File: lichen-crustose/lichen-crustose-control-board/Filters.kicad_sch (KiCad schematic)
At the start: 11 parts, among them J5 Thonkiconn_Mono_Audio_Jack, J6 Thonkiconn_Mono_Audio_Jack, U1 NSL-32SR3, U2 NS-32SR2

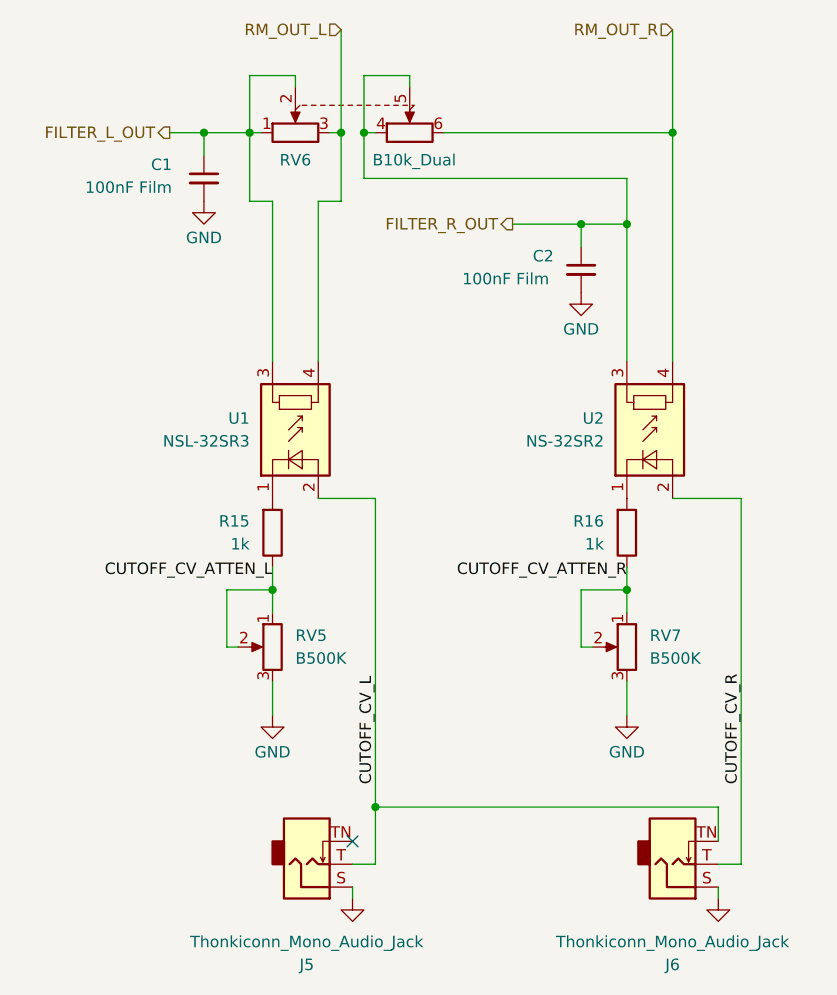
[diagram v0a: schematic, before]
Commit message: Updates Lichen symbols and footprints. Fixes to Crustose and Vactrol VCA. Adds 3D model of the RP2350 dual USB board.
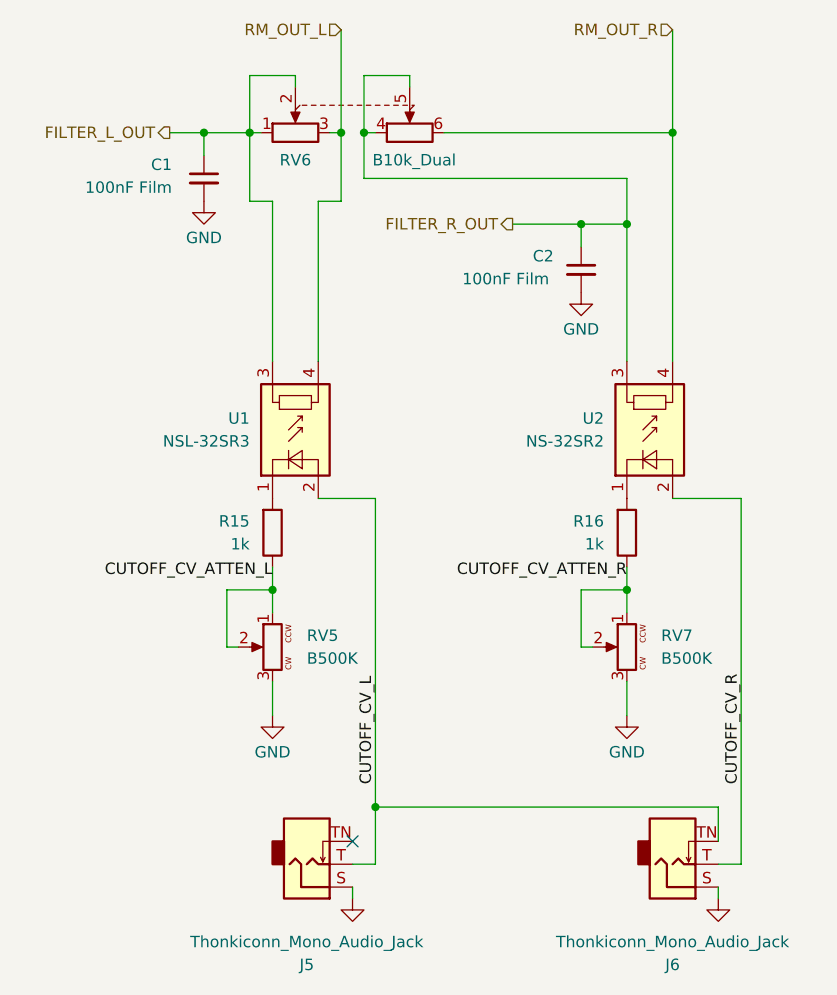
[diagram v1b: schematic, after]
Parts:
- J5, J6, RV6, U1, U2: now left out of the parts list
- R15, R16: value 10k_0603 -> 1k_0603; JLCPCB ID C25804 -> (none)
- RV5, RV7: symbol Lichen:Potentiometer -> Lichen:R_Potentiometer; now left out of the parts list
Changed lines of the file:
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@@
 		(unit 1)
 		(exclude_from_sim no)
-		(in_bom yes)
+		(in_bom no)
 		(on_board yes)
 		(dnp no)
@@
 		(unit 1)
 		(exclude_from_sim no)
-		(in_bom yes)
+		(in_bom no)
 		(on_board yes)
 		(dnp no)
@@
 		(unit 1)
 		(exclude_from_sim no)
-		(in_bom yes)
+		(in_bom no)
 		(on_board yes)
 		(dnp no)
@@
 	)
 	(symbol
-		(lib_id "Lichen:Potentiometer")
+		(lib_id "Lichen:R_Potentiometer")
 		(at 119.38 114.3 0)
 		(mirror y)
 		(unit 1)
 		(exclude_from_sim no)
-		(in_bom yes)
+		(in_bom no)
 		(on_board yes)
 		(dnp no)
 		(fields_autoplaced yes)
 		(property "Reference" "RV5"
-			(at 121.92 113.0299 0)
+			(at 123.19 113.0299 0)
 			(effects
 				(font
@@
 		)
 		(property "Value" "B500K"
-			(at 121.92 115.5699 0)
+			(at 123.19 115.5699 0)
 			(effects
 				(font
@@
 		(unit 1)
 		(exclude_from_sim no)
-		(in_bom yes)
+		(in_bom no)
 		(on_board yes)
 		(dnp no)
@@
 		(unit 1)
 		(exclude_from_sim no)
-		(in_bom yes)
+		(in_bom no)
 		(on_board yes)
 		(dnp no)
@@
 	)
 	(symbol
-		(lib_id "Lichen:Potentiometer")
+		(lib_id "Lichen:R_Potentiometer")
 		(at 158.75 114.3 0)
 		(mirror y)
 		(unit 1)
 		(exclude_from_sim no)
-		(in_bom yes)
+		(in_bom no)
 		(on_board yes)
 		(dnp no)
 		(fields_autoplaced yes)
 		(property "Reference" "RV7"
-			(at 161.29 113.0299 0)
+			(at 162.56 113.0299 0)
 			(effects
 				(font
@@
 		)
 		(property "Value" "B500K"
-			(at 161.29 115.5699 0)
+			(at 162.56 115.5699 0)
 			(effects
 				(font
@@
 			)
 		)
-		(property "Value" "10k_0603"
+		(property "Value" "1k_0603"
 			(at 156.21 101.6 90)
 			(effects
@@
 				)
 				(justify right)
-			)
-		)
-		(property "JLCPCB ID" "C25804"
-			(at 160.02 86.36 0)
-			(effects
-				(font
-					(size 1.27 1.27)
-				)
-				(hide yes)
 			)
 		)
@@
 			)
 		)
-		(property "Value" "10k_0603"
+		(property "Value" "1k_0603"
 			(at 116.84 101.6 90)
 			(effects
@@
 			)
 		)
-		(property "JLCPCB ID" "C25804"
-			(at 120.65 86.36 0)
-			(effects
-				(font
-					(size 1.27 1.27)
-				)
-				(hide yes)
-			)
-		)

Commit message: feat: Updates Crustose, Cladonia and YouMe Transformer. Adds Stereo Latencies.
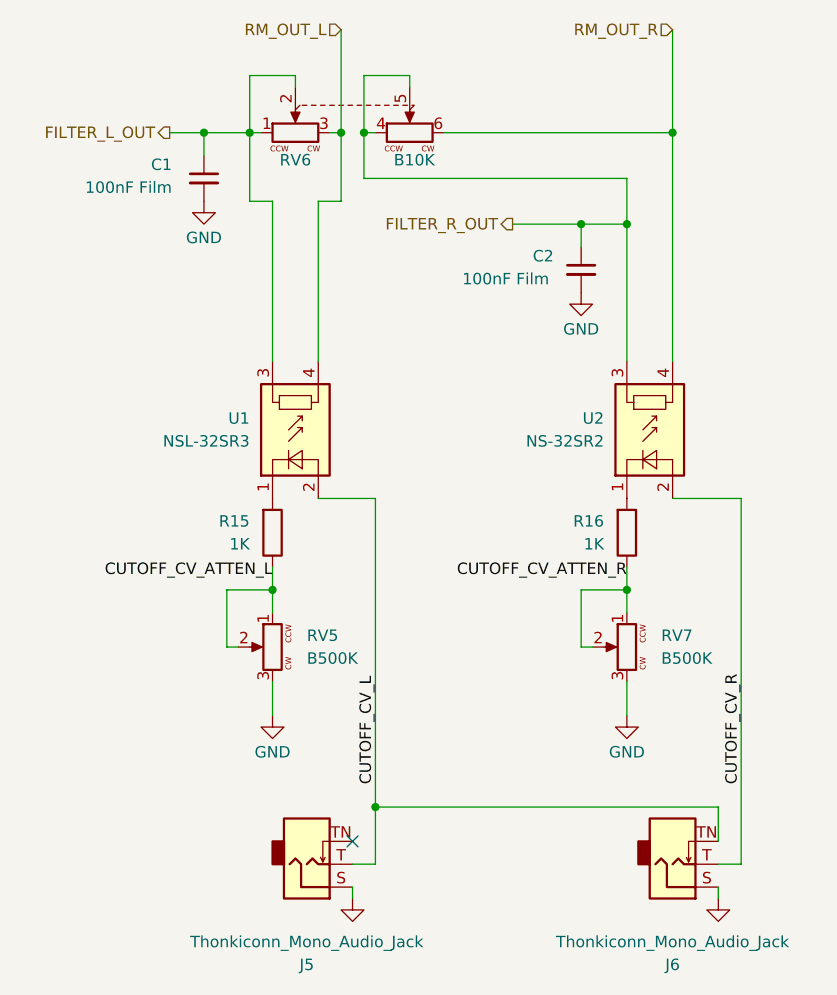
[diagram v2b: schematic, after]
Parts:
- R15, R16: value 1k_0603 -> 1K; Display 1k -> 1K
- RV6: value B10k_Dual -> B10K; symbol Lichen:10K_Potentiometer_Dual_Gang_Alpha_RD902F -> Lichen:R_Potentiometer_Dual
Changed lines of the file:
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@@
 	)
 	(symbol
-		(lib_id "Lichen:10K_Potentiometer_Dual_Gang_Alpha_RD902F")
+		(lib_id "Lichen:R_Potentiometer_Dual")
 		(at 128.27 54.61 0)
 		(unit 1)
@@
 			)
 		)
-		(property "Value" "B10k_Dual"
+		(property "Value" "B10K"
 			(at 135.128 60.198 0)
 			(effects
@@
 		)
 		(property "Footprint" "Lichen:Potentiometer_Alpha_RD902F-40-00D_Dual_Vertical"
-			(at 134.62 56.515 0)
+			(at 135.128 66.548 0)
 			(effects
 				(font
@@
 		)
 		(property "Datasheet" "https://www.thonk.co.uk/shop/alpha-9mm-pots-vert-t18-dual-gang/"
-			(at 134.62 56.515 0)
+			(at 134.874 63.754 0)
 			(effects
 				(font
@@
 		)
 		(property "Description" "Dual potentiometer"
-			(at 128.27 54.61 0)
+			(at 128.016 69.342 0)
 			(effects
 				(font
@@
 		)
 		(property "Manufacturer" "Alpha"
-			(at 128.27 54.61 90)
+			(at 128.27 71.882 0)
 			(effects
 				(font
@@
 		)
 		(property "Part Number" "RD90F-40"
-			(at 128.27 54.61 90)
+			(at 128.27 74.168 0)
 			(effects
 				(font
@@
 			)
 		)
-		(property "Value" "1k_0603"
+		(property "Value" "1K"
 			(at 156.21 101.6 90)
 			(effects
@@
 			)
 		)
-		(property "Datasheet" "https://www.lcsc.com/datasheet/lcsc_datasheet_2206010130_UNI-ROYAL-Uniroyal-Elec-0603WAF1001T5E_C21190.pdf"
+		(property "Datasheet" "https://jlcpcb.com/api/file/downloadByFileSystemAccessId/8579706098733010944"
 			(at 162.052 78.74 0)
 			(effects
@@
 			)
 		)
-		(property "Description" "1K, 1%, 1/10W, 0603"
+		(property "Description" "1kΩ 75V Thick Film Resistor ±1% ±100ppm/℃ 0603"
 			(at 159.766 81.534 0)
 			(effects
@@
 			)
 		)
-		(property "Display" "1k"
+		(property "Display" "1K"
 			(at 156.21 102.8699 0)
 			(effects
@@
 			)
 		)
-		(property "Value" "1k_0603"
+		(property "Value" "1K"
 			(at 116.84 101.6 90)
 			(effects
@@
 			)
 		)
-		(property "Datasheet" "https://www.lcsc.com/datasheet/lcsc_datasheet_2206010130_UNI-ROYAL-Uniroyal-Elec-0603WAF1001T5E_C21190.pdf"
+		(property "Datasheet" "https://jlcpcb.com/api/file/downloadByFileSystemAccessId/8579706098733010944"
 			(at 122.682 78.74 0)
 			(effects
@@
 			)
 		)
-		(property "Description" "1K, 1%, 1/10W, 0603"
+		(property "Description" "1kΩ 75V Thick Film Resistor ±1% ±100ppm/℃ 0603"
 			(at 120.396 81.534 0)
 			(effects
@@
 			)
 		)
-		(property "Display" "1k"
+		(property "Display" "1K"
 			(at 116.84 102.8699 0)
 			(effects
